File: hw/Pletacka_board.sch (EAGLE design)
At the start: 52 parts, among them U1 LM75BDP-NEW, U2 EL357N(A)(TA)-G, U3 EL357N(A)(TA)-G, U4 EL357N(A)(TA)-G, U5 EL357N(A)(TA)-G, U6 TPS54231D

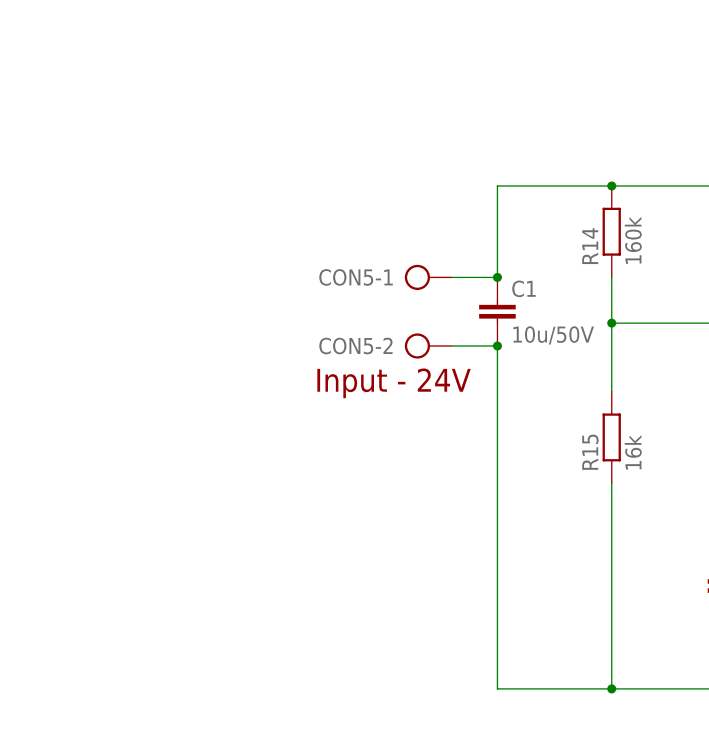
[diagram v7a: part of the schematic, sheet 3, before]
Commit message: Add PS reverse polarity & over. pr. (close #8)
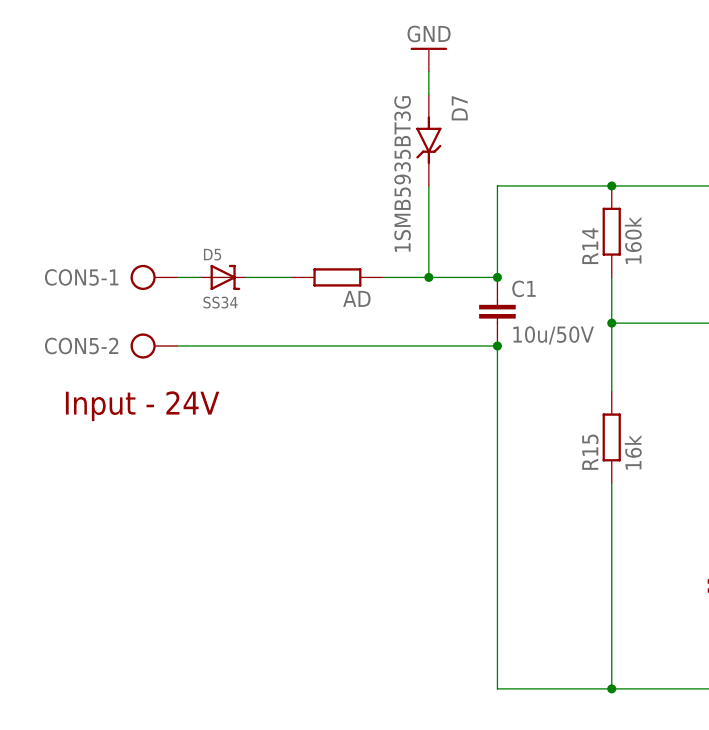
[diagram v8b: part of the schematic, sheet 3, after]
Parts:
- added AD: (no value), rcl_upravena:R-EU_R1206
- added D5: SS34, diode:SHOTTKY-SMA
- added D7: 1SMB5935BT3G, 1SMB5935BT3G:1SMB5935BT3G
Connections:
- new net N$3: CON5-1.KL, D5.A
- new net N$4: AD.2, D5.C
- net GND: now also D7.A
- net VIN: now also AD.1, D7.K; no longer CON5-1.KL
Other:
- moved on the sheet: CON5-1, CON5-2
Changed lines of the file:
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@@
 <attribute name="LCSC_ID" value="C8598"/>
 </part>
+<part name="D5" library="diode" deviceset="SHOTTKY" device="-SMA" value="SS34">
+<attribute name="LCSC_ID" value="C8678"/>
+</part>
+<part name="AD" library="rcl_upravena" deviceset="R-EU_" device="R1206">
+<spice>
+<pinmapping spiceprefix="R">
+<pinmap gate="G$1" pin="1" pinorder="1"/>
+<pinmap gate="G$1" pin="2" pinorder="2"/>
+</pinmapping>
+</spice>
+<attribute name="LCSC_ID" value="C22813"/>
+</part>
+<part name="GND14" library="supply1" library_urn="urn:adsk.eagle:library:371" deviceset="GND" device=""/>
+<part name="D7" library="1SMB5935BT3G" deviceset="1SMB5935BT3G" device=""/>
 </parts>
 <sheets>
@@
 <description>Power</description>
 <plain>
-<text x="40.64" y="83.82" size="2.54" layer="94">Input - 24V</text>
+<text x="12.7" y="81.28" size="2.54" layer="94">Input - 24V</text>
 </plain>
 <instances>
@@
 <attribute name="SHEET" x="230.505" y="5.08" size="2.54" layer="94"/>
 </instance>
-<instance part="CON5" gate="-1" x="50.8" y="96.52" smashed="yes">
-<attribute name="NAME" x="49.53" y="97.409" size="1.778" layer="95" rot="R180"/>
-</instance>
-<instance part="CON5" gate="-2" x="50.8" y="88.9" smashed="yes">
-<attribute name="NAME" x="49.53" y="89.789" size="1.778" layer="95" rot="R180"/>
-<attribute name="VALUE" x="46.99" y="85.217" size="1.778" layer="96"/>
+<instance part="CON5" gate="-1" x="20.32" y="96.52" smashed="yes">
+<attribute name="NAME" x="19.05" y="97.409" size="1.778" layer="95" rot="R180"/>
+</instance>
+<instance part="CON5" gate="-2" x="20.32" y="88.9" smashed="yes">
+<attribute name="NAME" x="19.05" y="89.789" size="1.778" layer="95" rot="R180"/>
+<attribute name="VALUE" x="16.51" y="85.217" size="1.778" layer="96"/>
 </instance>
 <instance part="C1" gate="G$1" x="60.96" y="93.98" smashed="yes">
@@
 <attribute name="VALUE" x="188.341" y="98.806" size="1.27" layer="96" rot="MR270"/>
 <attribute name="LCSC_ID" x="190.5" y="96.52" size="1.27" layer="96" rot="R270" display="off"/>
+</instance>
+<instance part="D5" gate="G$1" x="30.48" y="96.52" smashed="yes">
+<attribute name="NAME" x="28.194" y="98.425" size="1.27" layer="95"/>
+<attribute name="VALUE" x="28.194" y="94.361" size="1.27" layer="96" rot="MR180"/>
+<attribute name="LCSC_ID" x="30.48" y="96.52" size="1.27" layer="96" display="off"/>
+</instance>
+<instance part="AD" gate="G$1" x="43.18" y="96.52" smashed="yes" rot="R180">
+<attribute name="NAME" x="46.99" y="95.0214" size="1.778" layer="95" rot="R180"/>
+<attribute name="VALUE" x="46.99" y="99.822" size="1.778" layer="96" rot="R180"/>
+<attribute name="LCSC_ID" x="43.18" y="96.52" size="1.778" layer="96" rot="R180" display="off"/>
+</instance>
+<instance part="GND14" gate="1" x="53.34" y="121.92" smashed="yes" rot="R180">
+<attribute name="VALUE" x="55.88" y="124.46" size="1.778" layer="96" rot="R180"/>
+</instance>
+<instance part="D7" gate="G$1" x="53.34" y="111.76" smashed="yes" rot="R270">
+<attribute name="NAME" x="55.88" y="116.84" size="1.778" layer="95" rot="R270"/>
+<attribute name="VALUE" x="49.53" y="116.84" size="1.778" layer="96" rot="R270"/>
 </instance>
 </instances>
@@
 <net name="VIN" class="0">
 <segment>
-<pinref part="CON5" gate="-1" pin="KL"/>
 <pinref part="C1" gate="G$1" pin="1"/>
-<wire x1="55.88" y1="96.52" x2="60.96" y2="96.52" width="0.1524" layer="91"/>
 <wire x1="60.96" y1="96.52" x2="60.96" y2="106.68" width="0.1524" layer="91"/>
 <junction x="60.96" y="96.52"/>
@@
 <junction x="73.66" y="106.68"/>
 <label x="106.68" y="106.68" size="1.778" layer="95"/>
+<wire x1="48.26" y1="96.52" x2="53.34" y2="96.52" width="0.1524" layer="91"/>
+<pinref part="AD" gate="G$1" pin="1"/>
+<wire x1="53.34" y1="96.52" x2="60.96" y2="96.52" width="0.1524" layer="91"/>
+<wire x1="53.34" y1="96.52" x2="53.34" y2="106.68" width="0.1524" layer="91"/>
+<junction x="53.34" y="96.52"/>
+<pinref part="D7" gate="G$1" pin="K"/>
 </segment>
 </net>
 <net name="GND" class="0">
 <segment>
-<pinref part="CON5" gate="-2" pin="KL"/>
-<pinref part="C1" gate="G$1" pin="2"/>
-<wire x1="55.88" y1="88.9" x2="60.96" y2="88.9" width="0.1524" layer="91"/>
-<wire x1="60.96" y1="88.9" x2="60.96" y2="50.8" width="0.1524" layer="91"/>
-<junction x="60.96" y="88.9"/>
 <wire x1="60.96" y1="50.8" x2="73.66" y2="50.8" width="0.1524" layer="91"/>
 <wire x1="73.66" y1="50.8" x2="86.36" y2="50.8" width="0.1524" layer="91"/>
@@
 <wire x1="111.76" y1="58.42" x2="111.76" y2="50.8" width="0.1524" layer="91"/>
 <junction x="111.76" y="50.8"/>
+<pinref part="C1" gate="G$1" pin="2"/>
+<wire x1="60.96" y1="50.8" x2="60.96" y2="88.9" width="0.1524" layer="91"/>
+<pinref part="CON5" gate="-2" pin="KL"/>
+<wire x1="60.96" y1="88.9" x2="25.4" y2="88.9" width="0.1524" layer="91"/>
+<junction x="60.96" y="88.9"/>
 </segment>
 <segment>
@@
 <junction x="190.5" y="106.68"/>
 <pinref part="D3" gate="G$1" pin="A"/>
+</segment>
+<segment>
+<pinref part="GND14" gate="1" pin="GND"/>
+<pinref part="D7" gate="G$1" pin="A"/>
+<wire x1="53.34" y1="116.84" x2="53.34" y2="119.38" width="0.1524" layer="91"/>
 </segment>
 </net>
@@
 </segment>
 </net>
+<net name="N$3" class="0">
+<segment>
+<pinref part="CON5" gate="-1" pin="KL"/>
+<wire x1="25.4" y1="96.52" x2="27.94" y2="96.52" width="0.1524" layer="91"/>
+<pinref part="D5" gate="G$1" pin="A"/>
+</segment>
+</net>
+<net name="N$4" class="0">
+<segment>
+<pinref part="D5" gate="G$1" pin="C"/>
+<wire x1="33.02" y1="96.52" x2="38.1" y2="96.52" width="0.1524" layer="91"/>
+<pinref part="AD" gate="G$1" pin="2"/>
+</segment>
+</net>
